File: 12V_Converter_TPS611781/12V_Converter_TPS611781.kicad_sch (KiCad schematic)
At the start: 23 parts, among them M1 IQE050N08NM5CGSC, U1 LM51561HPWPR

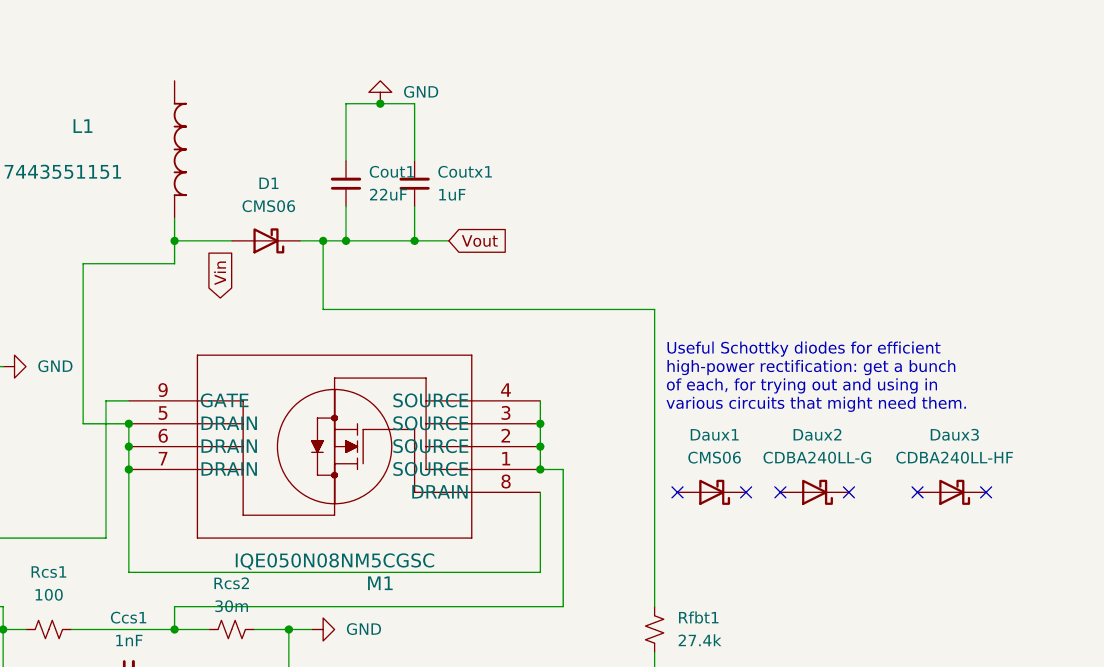
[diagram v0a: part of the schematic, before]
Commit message: reduced switching loop area
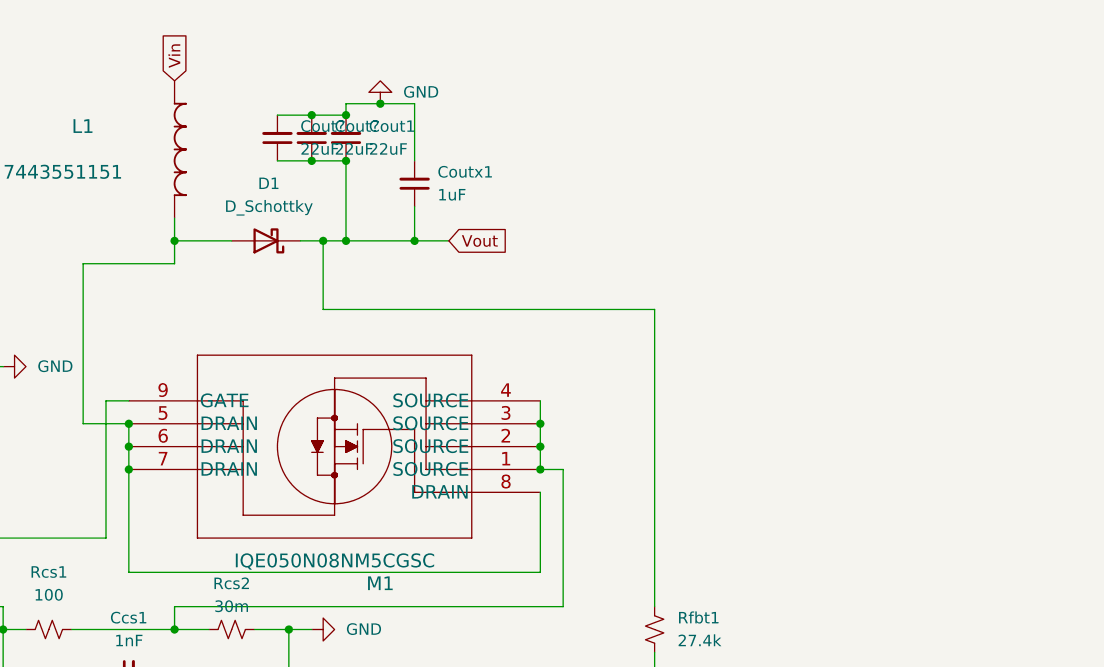
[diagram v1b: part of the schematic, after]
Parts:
- removed Daux1: CMS06, symbol Device:D_Schottky
- removed Daux2: CDBA240LL-G, symbol Device:D_Schottky
- removed Daux3: CDBA240LL-HF, symbol Device:D_Schottky
- added Cout? (x2): 22uF, Capacitor_SMD:C_1210_3225Metric, symbol Device:C_Small
- D1: value CMS06 -> D_Schottky
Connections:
- net GND: now also Cout?.2, Cout?.2
- net Vin: now also L1.2
- net Vout: now also Cout?.1, Cout?.1
- no-connect marks 8 -> 2
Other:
- note removed: "Useful Schottky diodes for efficient high-power rectification: get a bunch of each, for trying out and using in various circuits that might need them."
- moved on the sheet: Cout1
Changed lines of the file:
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@@
 (kicad_sch (version 20211123) (generator eeschema)
   (paper "A4")
+  (junction (at 189.23 44.45) (diameter 0) (color 0 0 0 0)
+  )
   (junction (at 196.85 38.1) (diameter 0) (color 0 0 0 0)
   )
@@
   (junction (at 168.91 73.66) (diameter 0) (color 0 0 0 0)
   )
+  (junction (at 189.23 39.37) (diameter 0) (color 0 0 0 0)
+  )
   (junction (at 186.69 101.6) (diameter 0) (color 0 0 0 0)
   )
+  (junction (at 193.04 44.45) (diameter 0) (color 0 0 0 0)
+  )
+  (junction (at 193.04 39.37) (diameter 0) (color 0 0 0 0)
+  )
   (junction (at 214.63 78.74) (diameter 0) (color 0 0 0 0)
   )
@@
   (junction (at 173.99 96.52) (diameter 0) (color 0 0 0 0)
   )
-  (no_connect (at 229.87 81.28))
-  (no_connect (at 237.49 81.28))
-  (no_connect (at 256.54 81.28))
-  (no_connect (at 248.92 81.28))
-  (no_connect (at 241.3 81.28))
-  (no_connect (at 264.16 81.28))
   (no_connect (at 100.33 101.6))
   (no_connect (at 100.33 124.46))
@@
     (stroke (width 0) (type default) (color 0 0 0 0))
   )
-  (wire (pts (xy 193.04 44.45) (xy 193.04 38.1))
+  (wire (pts (xy 193.04 39.37) (xy 193.04 38.1))
     (stroke (width 0) (type default) (color 0 0 0 0))
   )
@@
     (stroke (width 0) (type default) (color 0 0 0 0))
   )
+  (wire (pts (xy 189.23 44.45) (xy 193.04 44.45))
+    (stroke (width 0) (type default) (color 0 0 0 0))
+  )
   (wire (pts (xy 214.63 90.17) (xy 168.91 90.17))
     (stroke (width 0) (type default) (color 0 0 0 0))
@@
     (stroke (width 0) (type default) (color 0 0 0 0))
   )
-  (wire (pts (xy 193.04 49.53) (xy 193.04 53.34))
+  (wire (pts (xy 193.04 44.45) (xy 193.04 53.34))
     (stroke (width 0) (type default) (color 0 0 0 0))
   )
@@
     (stroke (width 0) (type default) (color 0 0 0 0))
   )
+  (wire (pts (xy 185.42 44.45) (xy 189.23 44.45))
+    (stroke (width 0) (type default) (color 0 0 0 0))
+  )
   (wire (pts (xy 154.94 93.98) (xy 152.4 93.98))
     (stroke (width 0) (type default) (color 0 0 0 0))
@@
     (stroke (width 0) (type default) (color 0 0 0 0))
   )
+  (wire (pts (xy 189.23 39.37) (xy 193.04 39.37))
+    (stroke (width 0) (type default) (color 0 0 0 0))
+  )
   (wire (pts (xy 81.28 78.74) (xy 92.71 78.74))
     (stroke (width 0) (type default) (color 0 0 0 0))
@@
     (stroke (width 0) (type default) (color 0 0 0 0))
   )
-  (text "Useful Schottky diodes for efficient\nhigh-power rectification: get a bunch\nof each, for trying out and using in\nvarious circuits that might need them."
-    (at 228.6 72.39 0)
-    (effects (font (size 1.27 1.27)) (justify left bottom))
-  )
-  (global_label "Vin" (shape input) (at 179.07 59.69 90) (fields_autoplaced)
+  (wire (pts (xy 185.42 39.37) (xy 189.23 39.37))
+    (stroke (width 0) (type default) (color 0 0 0 0))
+  )
+  (global_label "Vin" (shape input) (at 173.99 35.56 90) (fields_autoplaced)
     (effects (font (size 1.27 1.27)) (justify left))
     (property "Intersheet References" "${INTERSHEET_REFS}" (id 0) (at 174.0694 30.3045 90)
@@
     )
     (property "Datasheet" "~" (id 3) (at 186.69 110.49 0)
+      (effects (font (size 1.27 1.27)) hide)
+    )
+    (pin "1")
+    (pin "2")
+  )
+  (symbol (lib_id "Device:C_Small") (at 189.23 41.91 180) (unit 1)
+    (in_bom yes) (on_board yes) (fields_autoplaced)
+    (property "Reference" "Cout?" (id 0) (at 191.77 40.6335 0)
+      (effects (font (size 1.27 1.27)) (justify right))
+    )
+    (property "Value" "22uF" (id 1) (at 191.77 43.1735 0)
+      (effects (font (size 1.27 1.27)) (justify right))
+    )
+    (property "Footprint" "Capacitor_SMD:C_1210_3225Metric" (id 2) (at 189.23 41.91 0)
+      (effects (font (size 1.27 1.27)) hide)
+    )
+    (property "Datasheet" "~" (id 3) (at 189.23 41.91 0)
       (effects (font (size 1.27 1.27)) hide)
     )
@@
     (pin "1")
   )
+  (symbol (lib_id "Device:C_Small") (at 185.42 41.91 180) (unit 1)
+    (in_bom yes) (on_board yes) (fields_autoplaced)
+    (property "Reference" "Cout?" (id 0) (at 187.96 40.6335 0)
+      (effects (font (size 1.27 1.27)) (justify right))
+    )
+    (property "Value" "22uF" (id 1) (at 187.96 43.1735 0)
+      (effects (font (size 1.27 1.27)) (justify right))
+    )
+    (property "Footprint" "Capacitor_SMD:C_1210_3225Metric" (id 2) (at 185.42 41.91 0)
+      (effects (font (size 1.27 1.27)) hide)
+    )
+    (property "Datasheet" "~" (id 3) (at 185.42 41.91 0)
+      (effects (font (size 1.27 1.27)) hide)
+    )
+    (pin "1")
+    (pin "2")
+  )
   (symbol (lib_id "Device:C_Small") (at 149.86 67.31 90) (unit 1)
     (in_bom yes) (on_board yes) (fields_autoplaced)
@@
     )
     (pin "1")
-  )
-  (symbol (lib_id "Device:D_Schottky") (at 233.68 81.28 180) (unit 1)
-    (in_bom yes) (on_board no) (fields_autoplaced)
-    (property "Reference" "Daux1" (id 0) (at 233.9975 74.93 0))
-    (property "Value" "CMS06" (id 1) (at 233.9975 77.47 0))
-    (property "Footprint" "" (id 2) (at 233.68 81.28 0)
-      (effects (font (size 1.27 1.27)) hide)
-    )
-    (property "Datasheet" "~" (id 3) (at 233.68 81.28 0)
-      (effects (font (size 1.27 1.27)) hide)
-    )
-    (pin "1")
-    (pin "2")
   )
   (symbol (lib_id "Device:C_Small") (at 200.66 46.99 180) (unit 1)
@@
     (pin "2")
   )
-  (symbol (lib_id "Device:D_Schottky") (at 260.35 81.28 180) (unit 1)
-    (in_bom yes) (on_board no) (fields_autoplaced)
-    (property "Reference" "Daux3" (id 0) (at 260.6675 74.93 0))
-    (property "Value" "CDBA240LL-HF" (id 1) (at 260.6675 77.47 0))
-    (property "Footprint" "" (id 2) (at 260.35 81.28 0)
-      (effects (font (size 1.27 1.27)) hide)
-    )
-    (property "Datasheet" "~" (id 3) (at 260.35 81.28 0)
-      (effects (font (size 1.27 1.27)) hide)
-    )
-    (pin "1")
-    (pin "2")
-  )
   (symbol (lib_id "Device:R_Small_US") (at 93.98 109.22 90) (unit 1)
     (in_bom yes) (on_board yes)
@@
     (pin "2")
   )
-  (symbol (lib_id "Device:D_Schottky") (at 245.11 81.28 180) (unit 1)
-    (in_bom yes) (on_board no) (fields_autoplaced)
-    (property "Reference" "Daux2" (id 0) (at 245.4275 74.93 0))
-    (property "Value" "CDBA240LL-G" (id 1) (at 245.4275 77.47 0))
-    (property "Footprint" "" (id 2) (at 245.11 81.28 0)
-      (effects (font (size 1.27 1.27)) hide)
-    )
-    (property "Datasheet" "~" (id 3) (at 245.11 81.28 0)
-      (effects (font (size 1.27 1.27)) hide)
-    )
-    (pin "1")
-    (pin "2")
-  )
   (symbol (lib_id "Device:C_Small") (at 168.91 101.6 90) (unit 1)
     (in_bom yes) (on_board yes) (fields_autoplaced)
@@
     (pin "2")
   )
-  (symbol (lib_id "Device:C_Small") (at 193.04 46.99 180) (unit 1)
-    (in_bom yes) (on_board yes) (fields_autoplaced)
-    (property "Reference" "Cout1" (id 0) (at 195.58 45.7135 0)
-      (effects (font (size 1.27 1.27)) (justify right))
-    )
-    (property "Value" "22uF" (id 1) (at 195.58 48.2535 0)
-      (effects (font (size 1.27 1.27)) (justify right))
-    )
-    (property "Footprint" "Capacitor_SMD:C_1210_3225Metric" (id 2) (at 193.04 46.99 0)
-      (effects (font (size 1.27 1.27)) hide)
-    )
-    (property "Datasheet" "~" (id 3) (at 193.04 46.99 0)
+  (symbol (lib_id "Device:C_Small") (at 193.04 41.91 180) (unit 1)
+    (in_bom yes) (on_board yes) (fields_autoplaced)
+    (property "Reference" "Cout1" (id 0) (at 195.58 40.6335 0)
+      (effects (font (size 1.27 1.27)) (justify right))
+    )
+    (property "Value" "22uF" (id 1) (at 195.58 43.1735 0)
+      (effects (font (size 1.27 1.27)) (justify right))
+    )
+    (property "Footprint" "Capacitor_SMD:C_1210_3225Metric" (id 2) (at 193.04 41.91 0)
+      (effects (font (size 1.27 1.27)) hide)
+    )
+    (property "Datasheet" "~" (id 3) (at 193.04 41.91 0)
       (effects (font (size 1.27 1.27)) hide)
     )
@@
     (in_bom yes) (on_board yes) (fields_autoplaced)
     (property "Reference" "D1" (id 0) (at 184.4675 46.99 0))
-    (property "Value" "CMS06" (id 1) (at 184.4675 49.53 0))
+    (property "Value" "D_Schottky" (id 1) (at 184.4675 49.53 0))
     (property "Footprint" "Diode_SMD:D_SOD-128" (id 2) (at 184.15 53.34 0)
       (effects (font (size 1.27 1.27)) hide)
@@
       (reference "Cout1") (unit 1) (value "22uF") (footprint "Capacitor_SMD:C_1210_3225Metric")
     )
+    (path "/3703e8ca-52d6-47b5-89dc-0036da78ad40"
+      (reference "Cout?") (unit 1) (value "22uF") (footprint "Capacitor_SMD:C_1210_3225Metric")
+    )
+    (path "/733d0373-1ccd-42a3-952a-0ab52ee861ad"
+      (reference "Cout?") (unit 1) (value "22uF") (footprint "Capacitor_SMD:C_1210_3225Metric")
+    )
     (path "/99d7bd64-3387-4e95-847c-2de548d59b02"
       (reference "Coutx1") (unit 1) (value "1uF") (footprint "Capacitor_SMD:C_0805_2012Metric")
@@
     )
     (path "/f0bdfea9-aa78-4c8d-9d8f-d4a0a0c87be1"
-      (reference "D1") (unit 1) (value "CMS06") (footprint "Diode_SMD:D_SOD-128")
-    )
-    (path "/9779ce16-3c39-4fea-b79d-9c628c9fd4f0"
-      (reference "Daux1") (unit 1) (value "CMS06") (footprint "")
-    )
-    (path "/b8d64ab2-1148-4fd0-be52-89ce33214e76"
-      (reference "Daux2") (unit 1) (value "CDBA240LL-G") (footprint "")
-    )
-    (path "/b14663c6-3479-459d-b6fd-32a79b733e7a"
-      (reference "Daux3") (unit 1) (value "CDBA240LL-HF") (footprint "")
+      (reference "D1") (unit 1) (value "D_Schottky") (footprint "Diode_SMD:D_SOD-128")
     )
     (path "/ac109eb7-5b8e-4633-8f87-344581a18086"

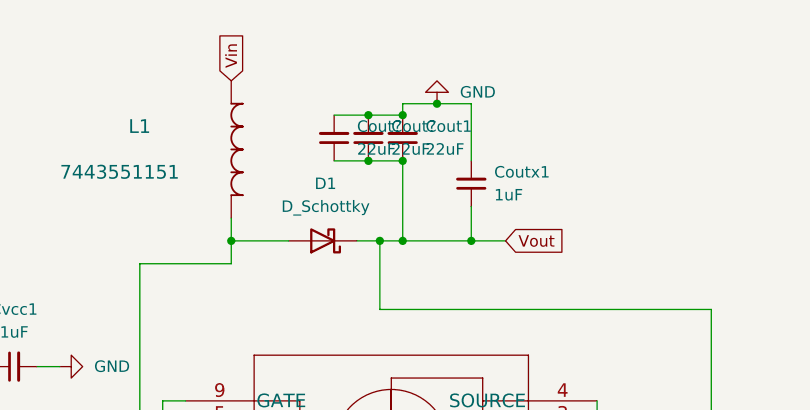
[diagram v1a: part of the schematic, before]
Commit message: corrected vin location on schematic
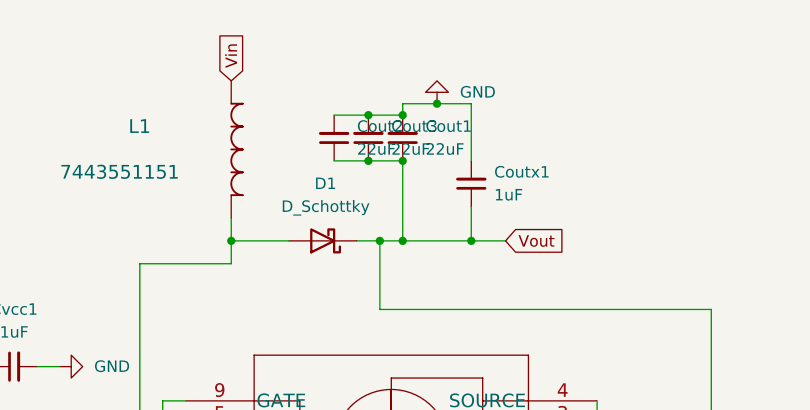
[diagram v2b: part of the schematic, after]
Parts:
- gave numbers to parts that had none: 2
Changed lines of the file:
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@@
   (symbol (lib_id "Device:C_Small") (at 189.23 41.91 180) (unit 1)
     (in_bom yes) (on_board yes) (fields_autoplaced)
-    (property "Reference" "Cout?" (id 0) (at 191.77 40.6335 0)
+    (property "Reference" "Cout3" (id 0) (at 191.77 40.6335 0)
       (effects (font (size 1.27 1.27)) (justify right))
     )
@@
   (symbol (lib_id "Device:C_Small") (at 185.42 41.91 180) (unit 1)
     (in_bom yes) (on_board yes) (fields_autoplaced)
-    (property "Reference" "Cout?" (id 0) (at 187.96 40.6335 0)
+    (property "Reference" "Cout2" (id 0) (at 187.96 40.6335 0)
       (effects (font (size 1.27 1.27)) (justify right))
     )
@@
       (reference "Cout1") (unit 1) (value "22uF") (footprint "Capacitor_SMD:C_1210_3225Metric")
     )
+    (path "/733d0373-1ccd-42a3-952a-0ab52ee861ad"
+      (reference "Cout2") (unit 1) (value "22uF") (footprint "Capacitor_SMD:C_1210_3225Metric")
+    )
     (path "/3703e8ca-52d6-47b5-89dc-0036da78ad40"
-      (reference "Cout?") (unit 1) (value "22uF") (footprint "Capacitor_SMD:C_1210_3225Metric")
-    )
-    (path "/733d0373-1ccd-42a3-952a-0ab52ee861ad"
-      (reference "Cout?") (unit 1) (value "22uF") (footprint "Capacitor_SMD:C_1210_3225Metric")
+      (reference "Cout3") (unit 1) (value "22uF") (footprint "Capacitor_SMD:C_1210_3225Metric")
     )
     (path "/99d7bd64-3387-4e95-847c-2de548d59b02"

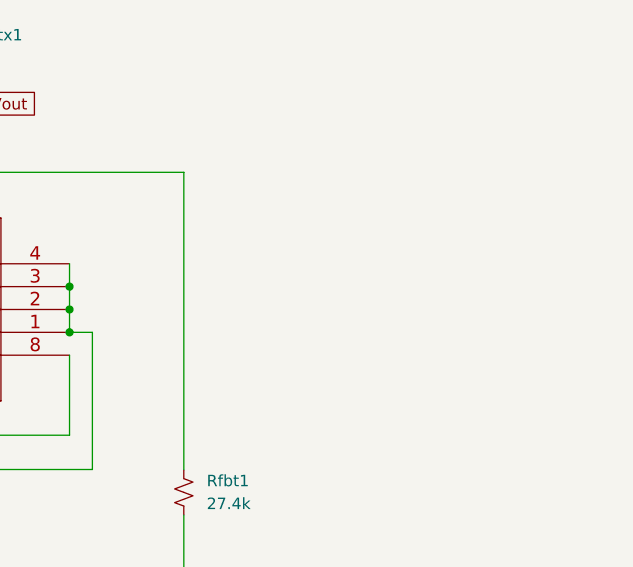
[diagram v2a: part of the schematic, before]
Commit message: added back the auxiliary diodes, which got annhialated for some reason
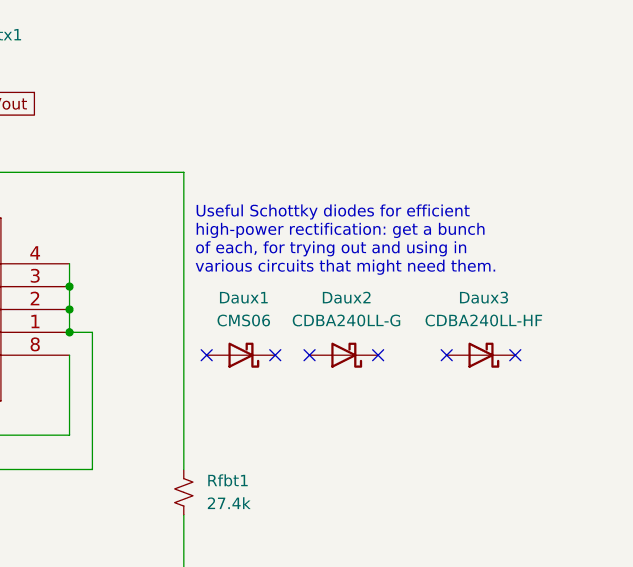
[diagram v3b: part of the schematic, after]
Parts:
- added Daux1: CMS06, symbol Device:D_Schottky
- added Daux2: CDBA240LL-G, symbol Device:D_Schottky
- added Daux3: CDBA240LL-HF, symbol Device:D_Schottky
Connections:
- no-connect marks 2 -> 8
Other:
- note added: "Useful Schottky diodes for efficient high-power rectification: get a bunch of each, for trying out and using in various circuits that might need them."
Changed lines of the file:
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@@
     )
   )
+  (no_connect (at 229.87 81.28))
+  (no_connect (at 237.49 81.28))
+  (no_connect (at 256.54 81.28))
+  (no_connect (at 248.92 81.28))
+  (no_connect (at 241.3 81.28))
+  (no_connect (at 264.16 81.28))
+  (text "Useful Schottky diodes for efficient\nhigh-power rectification: get a bunch\nof each, for trying out and using in\nvarious circuits that might need them."
+    (at 228.6 72.39 0)
+    (effects (font (size 1.27 1.27)) (justify left bottom))
 )
+    (symbol (lib_id "Device:D_Schottky") (at 233.68 81.28 180) (unit 1)
+    (in_bom yes) (on_board no) (fields_autoplaced)
+    (property "Reference" "Daux1" (id 0) (at 233.9975 74.93 0))
+    (property "Value" "CMS06" (id 1) (at 233.9975 77.47 0))
+    (property "Footprint" "" (id 2) (at 233.68 81.28 0)
+      (effects (font (size 1.27 1.27)) hide)
+    )
+    (property "Datasheet" "~" (id 3) (at 233.68 81.28 0)
+      (effects (font (size 1.27 1.27)) hide)
+    )
+    (pin "1")
+    (pin "2")
+  )
+  (symbol (lib_id "Device:D_Schottky") (at 260.35 81.28 180) (unit 1)
+    (in_bom yes) (on_board no) (fields_autoplaced)
+    (property "Reference" "Daux3" (id 0) (at 260.6675 74.93 0))
+    (property "Value" "CDBA240LL-HF" (id 1) (at 260.6675 77.47 0))
+    (property "Footprint" "" (id 2) (at 260.35 81.28 0)
+      (effects (font (size 1.27 1.27)) hide)
+    )
+    (property "Datasheet" "~" (id 3) (at 260.35 81.28 0)
+      (effects (font (size 1.27 1.27)) hide)
+    )
+    (pin "1")
+    (pin "2")
+  )
+  (symbol (lib_id "Device:D_Schottky") (at 245.11 81.28 180) (unit 1)
+    (in_bom yes) (on_board no) (fields_autoplaced)
+    (property "Reference" "Daux2" (id 0) (at 245.4275 74.93 0))
+    (property "Value" "CDBA240LL-G" (id 1) (at 245.4275 77.47 0))
+    (property "Footprint" "" (id 2) (at 245.11 81.28 0)
+      (effects (font (size 1.27 1.27)) hide)
+    )
+    (property "Datasheet" "~" (id 3) (at 245.11 81.28 0)
+      (effects (font (size 1.27 1.27)) hide)
+    )
+    (pin "1")
+    (pin "2")
+  )
+)
